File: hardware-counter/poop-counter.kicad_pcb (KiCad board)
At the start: 2 copper layers, 35 parts, among them J1 USB_C_Receptacle_USB2.0, J2 RJ12, U0 ESP8266EX, U1 AMS1117-3.3, U2 CP2102N-A01-GQFN24, U3 MAX485E, U4 W25Q32JVSS, Y1 24Mhz±10ppm

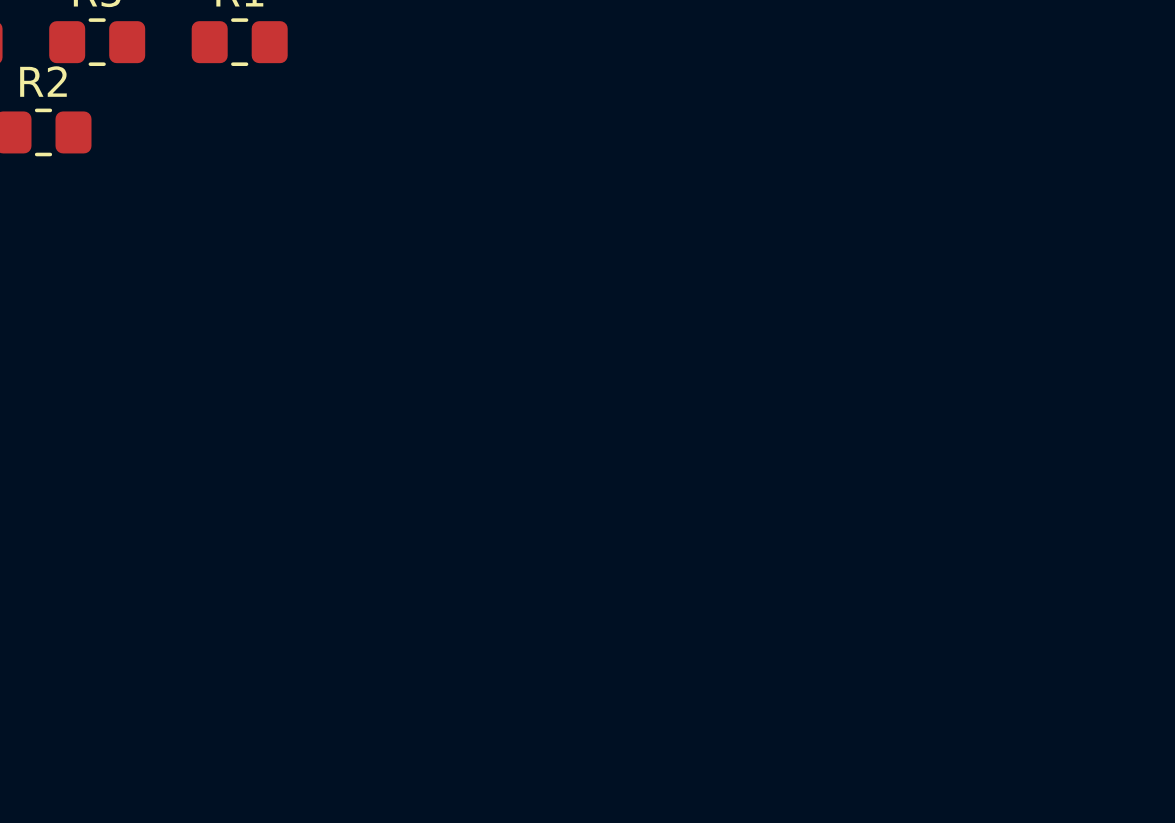
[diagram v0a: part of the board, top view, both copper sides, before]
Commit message: bout to remove USB
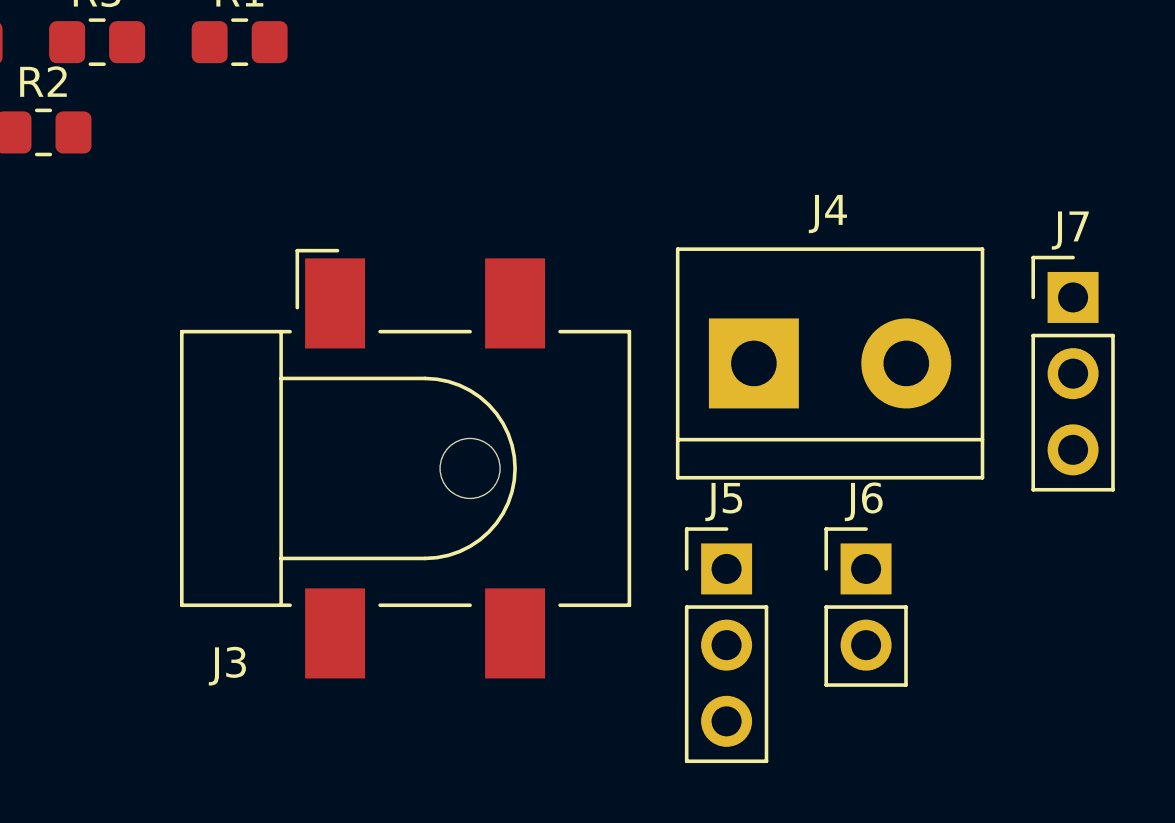
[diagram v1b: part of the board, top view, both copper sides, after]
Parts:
- added J3: Barrel_Jack, Connector_BarrelJack:BarrelJack_CLIFF_FC681465S_SMT_Horizontal, F.Cu at (172.1, 108.4)
- added J4: Screw_Terminal_01x02, TerminalBlock:TerminalBlock_bornier-2_P5.08mm, F.Cu at (183.0, 104.9)
- added J5: Conn_01x03_Male, Connector_PinHeader_2.54mm:PinHeader_1x03_P2.54mm_Vertical, F.Cu at (182.1, 111.8)
- added J6: Conn_01x02_Male, Connector_PinHeader_2.54mm:PinHeader_1x02_P2.54mm_Vertical, F.Cu at (186.8, 111.8)
- added J7: Conn_01x03_Male, Connector_PinHeader_2.54mm:PinHeader_1x03_P2.54mm_Vertical, F.Cu at (193.7, 102.7)
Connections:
- J1 pad A8: no_connect_43 -> no_connect_52
- J1 pad B8: no_connect_44 -> no_connect_53
- J1 pad S1: no_connect_45 -> no_connect_54
- J2 pad 1: no_connect_46 -> no_connect_55
- J2 pad 6: no_connect_47 -> no_connect_56
- U0 pad 5: no_connect_48 -> no_connect_57
- U2 pad 1: no_connect_49 -> no_connect_58
- U2 pad 11: no_connect_50 -> no_connect_59
- U2 pad 12: no_connect_51 -> no_connect_60
- U2 pad 15: no_connect_52 -> no_connect_61
- U2 pad 17: no_connect_53 -> no_connect_62
- U2 pad 18: no_connect_54 -> no_connect_63
- U2 pad 19: no_connect_55 -> no_connect_64
- U2 pad 22: no_connect_56 -> no_connect_65
- U2 pad 23: no_connect_57 -> no_connect_66
- U2 pad 24: no_connect_58 -> no_connect_67
- U2 pad 9: no_connect_59 -> no_connect_68
- U3 pad 1: no_connect_60 -> no_connect_69
- U3 pad 2: no_connect_61 -> no_connect_70

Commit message: done v1, need to redo routing entirely lol
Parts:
- removed D1: LED1, LED_SMD:LED_0805_2012Metric_Pad1.15x1.40mm_HandSolder
- removed D2: LED2, LED_SMD:LED_0805_2012Metric_Pad1.15x1.40mm_HandSolder
- removed the J1 at (142.6, 84.0)
- removed R10: 499, Resistor_SMD:R_0805_2012Metric_Pad1.20x1.40mm_HandSolder
- removed the R4 at (169.9, 87.4)
- removed R5: 22.1k, Resistor_SMD:R_0805_2012Metric_Pad1.20x1.40mm_HandSolder
- removed R6: 47.5k, Resistor_SMD:R_0805_2012Metric_Pad1.20x1.40mm_HandSolder
- removed R7, R8: 1k, Resistor_SMD:R_0805_2012Metric_Pad1.20x1.40mm_HandSolder
- removed the U2 at (141.1, 107.8)
- added C13: 0.33uF, Capacitor_SMD:C_0805_2012Metric_Pad1.18x1.45mm_HandSolder, F.Cu at (107.5, 104.8)
- added C14: 0.1uF, Capacitor_SMD:C_0805_2012Metric_Pad1.18x1.45mm_HandSolder, F.Cu at (116.2, 112.4)
- added U5: LM7805_TO220, Package_TO_SOT_THT:TO-220-3_Vertical, F.Cu at (111.3, 108.7)
- R3: value 5.1k -> 1k
- Y1: footprint Crystal:Crystal_SMD_3225-4Pin_3.2x2.5mm_HandSoldering -> Crystal:Crystal_SMD_EuroQuartz_X22-4Pin_2.5x2.0mm
- moved J5 88.8 mm to (94.4, 98.7), turned to 90 degrees
- moved J2 78.5 mm to (104.8, 98.1), turned to 180 degrees
- moved J6 73.1 mm to (98.9, 109.3)
- moved J3 70.8 mm to (123.0, 98.0), turned to 90 degrees
- moved J4 60.4 mm to (126.7, 106.0), turned to -90 degrees
- moved R1 55.7 mm to (110.7, 83.5), turned to 90 degrees
- moved C1 48.1 mm to (129.1, 113.0), turned to -90 degrees
- moved C2 44.7 mm to (117.0, 115.5), turned to 180 degrees
- moved R3 44.4 mm to (107.7, 96.8), turned to -90 degrees
- moved C11 44.1 mm to (113.6, 101.6), turned to 180 degrees
- moved C5 41.2 mm to (120.3, 85.5), turned to 180 degrees
- moved U4 40.6 mm to (114.7, 95.0), turned to -90 degrees
- moved R4 40.3 mm to (119.0, 97.7), turned to 90 degrees
- moved R2 38.8 mm to (127.1, 94.8)
- moved C8 35.3 mm to (134.2, 92.5), turned to 90 degrees
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- renumbered C2 to C1, C1 to C2, J2 to J1, J5 to J2, J7 to J3, J6 to J4, J4 to J5, J3 to J6, R11 to R1, R1 to R2, R2 to R4, U3 to U2
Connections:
- net Net-(U0-Pad10) renamed no_connect_25
- net Net-(U0-Pad12) renamed no_connect_26
- net Net-(U0-Pad16) renamed no_connect_27
- net Net-(U0-Pad24) renamed no_connect_28
- net Net-(U0-Pad32) renamed no_connect_29
- net Net-(U0-Pad6) renamed no_connect_31
- net Net-(U0-Pad7) renamed no_connect_32
- net Net-(U0-Pad8) renamed no_connect_33
- net Net-(U0-Pad9) renamed no_connect_34
- net no_connect_55 renamed no_connect_23
- net no_connect_56 renamed no_connect_24
- net no_connect_57 renamed no_connect_30
- net no_connect_69 renamed no_connect_35
- net no_connect_70 renamed no_connect_36
- C11 pad 1: MCU_VDDA -> +3V3
- C12 pad 1: MCU_VDDA -> +3V3
- C2 pad 1: MCU_VDDA -> +3V3
- C3 pad 1: MCU_VDDA -> +3V3
- C4 pad 1: MCU_VDDA -> +3V3
- C6 pad 1: MCU_VDDA -> +3V3
- J2 pad 1: Net-(J5-Pad1) -> +3V3
- J2 pad 2: Net-(J5-Pad2) -> GPIO0
- J2 pad 3: Net-(J5-Pad3) -> GND
- J3 pad 1: Net-(J7-Pad1) -> MCU_RX
- J3 pad 2: Net-(J7-Pad2) -> MCU_TX
- J3 pad 3: Net-(J7-Pad3) -> GND
- J4 pad 1: Net-(J6-Pad1) -> +5V
- J4 pad 2: Net-(J6-Pad2) -> GND
- L1 pad 1: MCU_VDDA -> +3V3
- R3 pad 1: Net-(J1-PadB5) -> GPIO0
- R3 pad 2: GND -> +3V3
- U0 pad 1: MCU_VDDA -> +3V3
- U0 pad 11: MCU_VDDA -> +3V3
- U0 pad 13: Net-(U0-Pad13) -> GND
- U0 pad 14: MCU_OUT_TX -> +3V3
- U0 pad 15: Net-(U0-Pad15) -> GPIO0
- U0 pad 17: MCU_VDDA -> +3V3
- U0 pad 29: MCU_VDDA -> +3V3
- U0 pad 30: MCU_VDDA -> +3V3
- U1 pad 3: MCU_VDDA -> +3V3
- U2 pad 4: MCU_OUT_TX -> MCU_TX
- U4 pad 8: MCU_VDDA -> +3V3
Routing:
- net +5V: track 0.00 -> 69.5 mm, vias 0 -> 1
- net MCU_TX: track 0.00 -> 57.6 mm, vias 0 -> 2
- net GND: track 0.00 -> 38.8 mm, vias 0 -> 20
- net +3V3: track 0.00 -> 37.9 mm, vias 0 -> 8
- net +24V: track 0.00 -> 27.4 mm
- net GPIO0: track 0.00 -> 21.3 mm, vias 0 -> 2
- net ROM_DI: track 0.00 -> 15.2 mm, vias 0 -> 2
- net OSC_OUT: track 0.00 -> 14.8 mm
- net RS485-: track 0.00 -> 14.0 mm, vias 0 -> 2
- net ROM_WP: track 0.00 -> 12.6 mm
- net RS485+: track 0.00 -> 12.4 mm
- net OSC_IN: track 0.00 -> 11.7 mm
- net ROM_DO: track 0.00 -> 11.5 mm
- net ROM_RST: track 0.00 -> 10.1 mm, vias 0 -> 2
- net MCU_VDD3P3: track 0.00 -> 8.63 mm, vias 0 -> 2
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- added copper zone on In2.Cu, net +3V3
- added copper zone on In1.Cu, net GND
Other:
- board outline added: 45.8 x 45.5 mm
- copper layers 2 -> 4
